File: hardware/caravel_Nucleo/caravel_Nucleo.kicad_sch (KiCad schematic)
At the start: 91 parts, among them J1 USB_B_Micro - 10118193-0001LF, J10 Conn_01x11_Female, J11 Conn_01x02, J12 Conn_01x02_Male, J2 Conn_01x02_Female, J3 Conn_01x02_Male, J4 Conn_01x04_Female, J5 Conn_01x02_Male, J6 Conn_01x02_Male, J7 Conn_01x06_Female, J8 Conn_01x03, J9 Conn_01x03, SW1 SW_Push - SKQGADE010, T1 Logo, T2 Logo, U1 FT232H, U10 MCP4661, U11 TAR5SxxU_SOT353F, U12 NUCLEO144-F746ZG, U2 SN74LVC1G125DCKR, U3 SN74LVC1G125DCKR, U4 MCP1319MT-29LE-OT, U5 TAR5SxxU_SOT353F, U6 TAR5SxxU_SOT353F, U7 W25Q32FVSS, U8 caravel_breakout, U9 MIC2211-AAYML-TR, X1 DSC6001_10MHZ, Y1 CSTNE12M0GH5L000R0

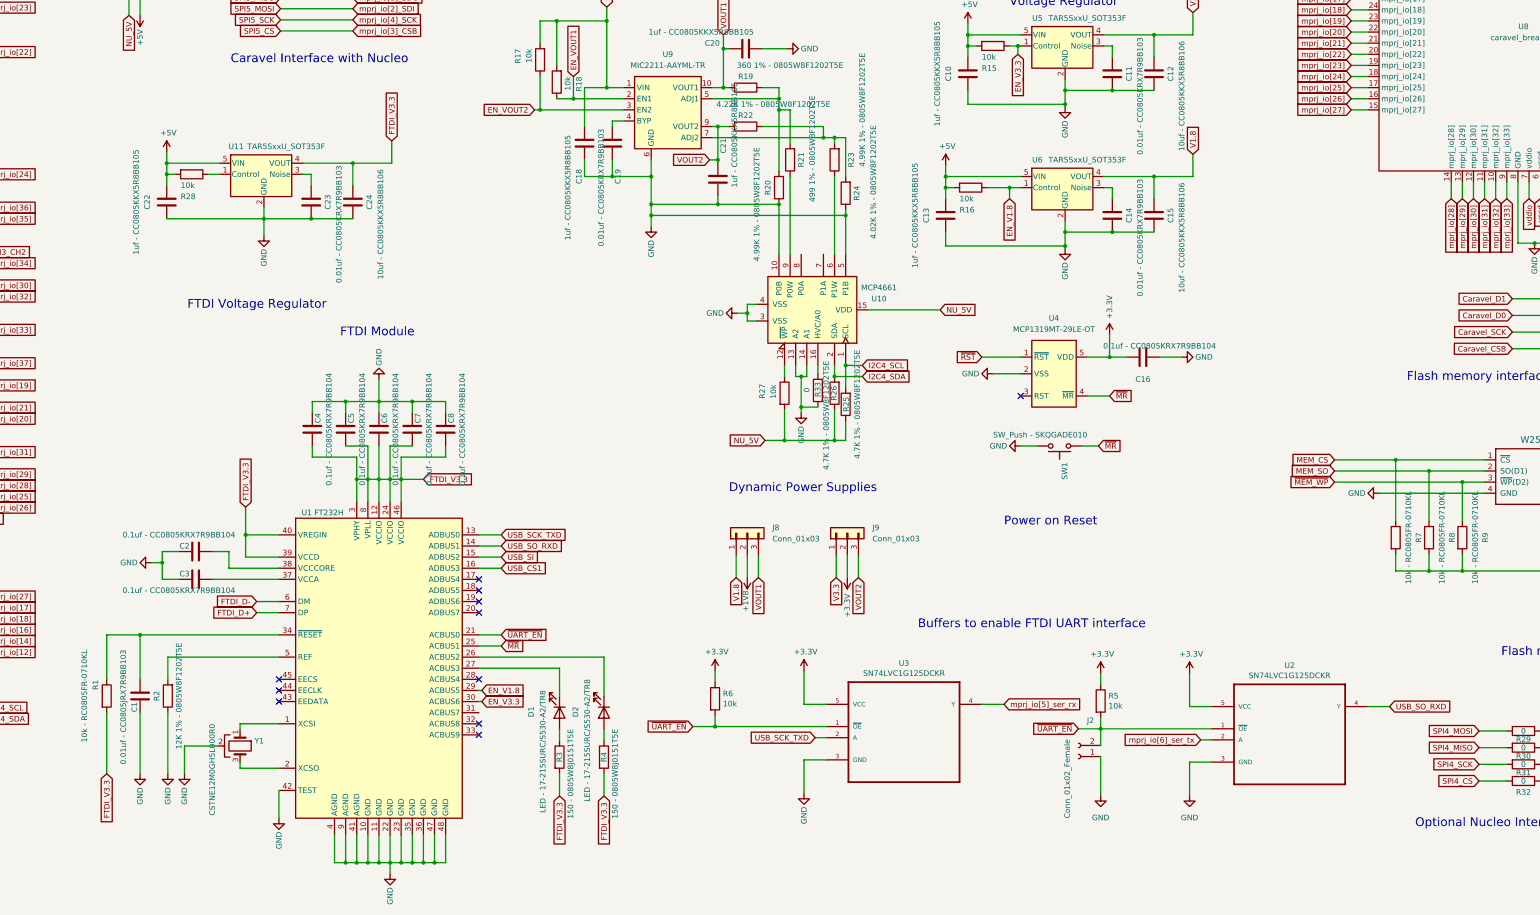
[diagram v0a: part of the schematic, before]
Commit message: Isolate FTDI scheamtic
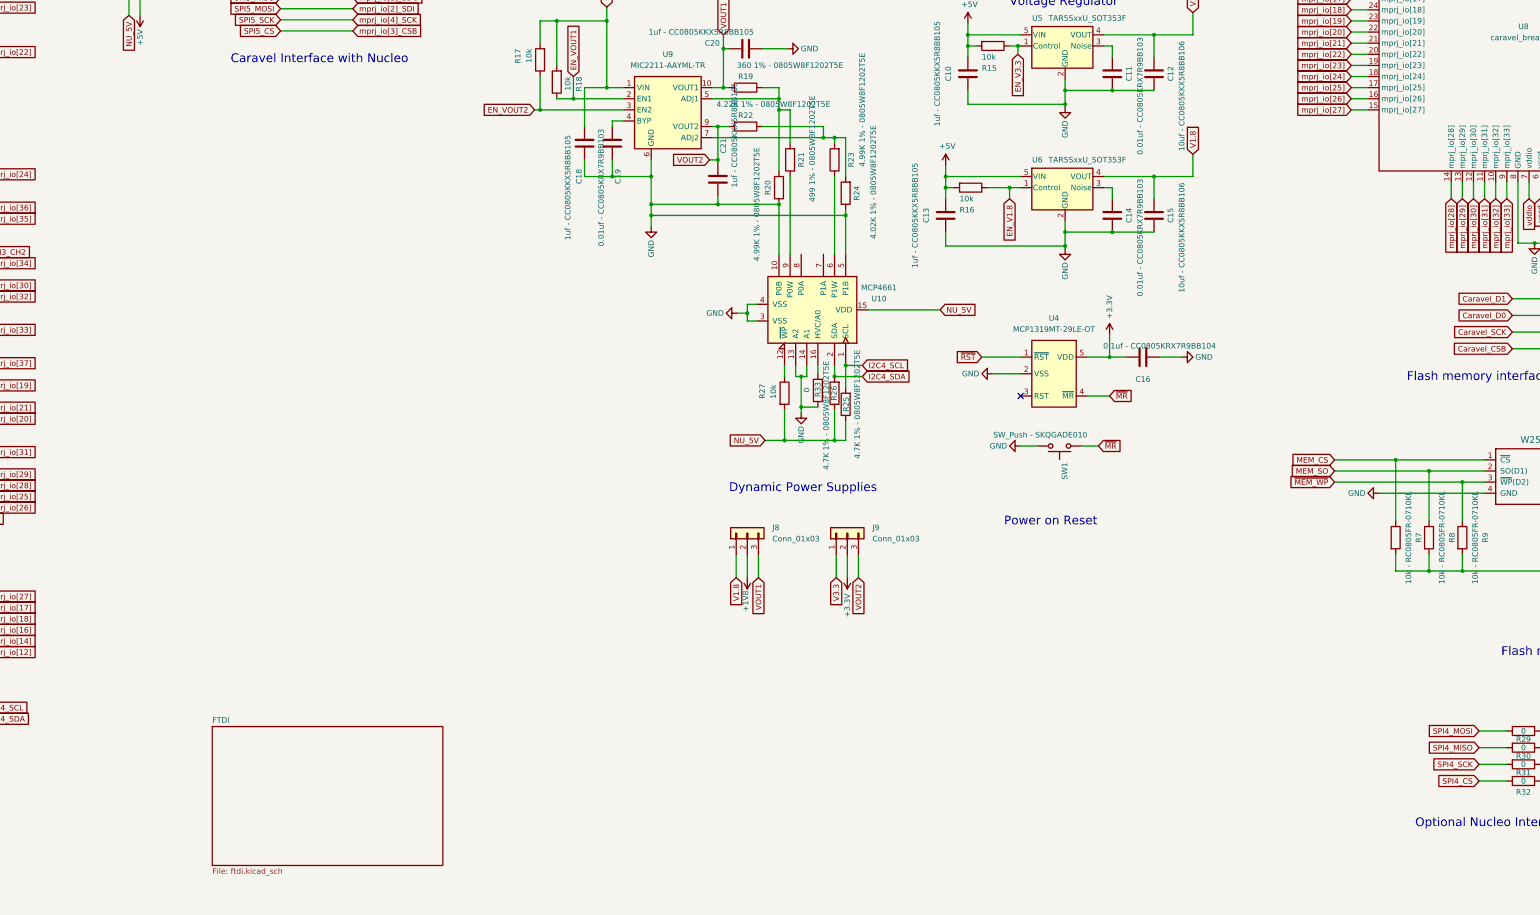
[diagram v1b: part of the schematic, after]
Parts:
- removed C1: 0.01uf - CC0805JRX7R9BB103, Capacitor_SMD:C_0805_2012Metric, symbol Device:C
- removed C2, C3, C4, C5, C6, C7, C8: 0.1uf - CC0805KRX7R9BB104, Capacitor_SMD:C_0805_2012Metric, symbol Device:C
- removed C22: 1uf - CC0805KKX5R8BB105, Capacitor_SMD:C_0805_2012Metric, symbol Device:C
- removed C23: 0.01uf - CC0805KRX7R9BB103, Capacitor_SMD:C_0805_2012Metric, symbol Device:C
- removed C24: 10uf - CC0805KKX5R8BB106, Capacitor_SMD:C_0805_2012Metric, symbol Device:C
- removed D1, D2: LED - 17-215SURC/S530-A2/TR8, LED_SMD:LED_1206_3216Metric, symbol Device:LED
- removed J2: Conn_01x02_Female, Connector_PinHeader_2.54mm:PinHeader_1x02_P2.54mm_Vertical, symbol Connector:Conn_01x02_Female
- removed R1: 10k - RC0805FR-0710KL, Resistor_SMD:R_0805_2012Metric, symbol Device:R
- removed R2: 12K 1% - 0805W8F1202T5E, Resistor_SMD:R_0805_2012Metric, symbol Device:R
- removed R28, R5, R6: 10k, Resistor_SMD:R_0805_2012Metric, symbol Device:R
- removed R3, R4: 150 - 0805W8J0151T5E, Resistor_SMD:R_0805_2012Metric, symbol Device:R
- removed U1: FT232H, Package_DFN_QFN:QFN-48-1EP_8x8mm_P0.5mm_EP6.2x6.2mm, symbol Interface_USB:FT232H
- removed U11: TAR5SxxU_SOT353F, Caravel_Board:SOT-353F, symbol Caravel_board:TAR5SxxU_SOT353F
- removed U2, U3: SN74LVC1G125DCKR, SOT65P210X110-5N, symbol Caravel_board:SN74LVC1G125DCKR
- removed Y1: CSTNE12M0GH5L000R0, strive_foot_prints:CSTNE12M0GH5L000R0, symbol Device:Crystal_GND2
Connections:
- no-connect marks 48 -> 38
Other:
- added sheet FTDI (ftdi.kicad_sch)
- note removed: "Buffers to enable FTDI UART interface"
- note removed: "FTDI Module"
- note removed: "FTDI Voltage Regulator"

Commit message: Substituted all components from main schematic sheet except Nucleo connector
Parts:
- removed C10, C13, C18, C20, C21: 1uf - CC0805KKX5R8BB105, Capacitor_SMD:C_0805_2012Metric, symbol Device:C
- removed C11, C14, C19: 0.01uf - CC0805KRX7R9BB103, Capacitor_SMD:C_0805_2012Metric, symbol Device:C
- removed C12, C15: 10uf - CC0805KKX5R8BB106, Capacitor_SMD:C_0805_2012Metric, symbol Device:C
- removed C16, C17, C9: 0.1uf - CC0805KRX7R9BB104, Capacitor_SMD:C_0805_2012Metric, symbol Device:C
- removed D3, D4: LED - 17-215SURC/S530-A2/TR8, LED_SMD:LED_1206_3216Metric, symbol Device:LED
- removed J1: USB_B_Micro - 10118193-0001LF, strive_foot_prints:FCI_10118193-0001LF, symbol Connector:USB_B_Micro
- removed J10: Conn_01x11_Female, Connector_PinHeader_2.54mm:PinHeader_1x11_P2.54mm_Vertical, symbol Connector:Conn_01x11_Female
- removed J11: Conn_01x02, Connector_PinHeader_2.54mm:PinHeader_1x02_P2.54mm_Vertical, symbol Connector_Generic:Conn_01x02
- removed J12, J3, J5, J6: Conn_01x02_Male, Connector_PinHeader_2.54mm:PinHeader_1x02_P2.54mm_Vertical, symbol Connector:Conn_01x02_Male
- removed J4: Conn_01x04_Female, Connector_PinHeader_2.54mm:PinHeader_1x04_P2.54mm_Vertical, symbol Connector:Conn_01x04_Female
- removed J7: Conn_01x06_Female, Connector_PinHeader_2.54mm:PinHeader_1x06_P2.54mm_Vertical, symbol Connector:Conn_01x06_Female
- removed J8, J9: Conn_01x03, Connector_PinHeader_2.54mm:PinHeader_1x03_P2.54mm_Vertical, symbol Connector_Generic:Conn_01x03
- removed R10, R11, R12, R7, R8, R9: 10k - RC0805FR-0710KL, Resistor_SMD:R_0805_2012Metric, symbol Device:R
- removed R13, R14: 82 - 0805W8F820JT5E, Resistor_SMD:R_0805_2012Metric, symbol Device:R
- removed R15, R16, R17, R18, R27: 10k, Resistor_SMD:R_0805_2012Metric, symbol Device:R
- removed R19: 360 1% - 0805W8F1202T5E, Resistor_SMD:R_0805_2012Metric, symbol Device:R
- removed R20, R23: 4.99K 1% - 0805W8F1202T5E, Resistor_SMD:R_0805_2012Metric, symbol Device:R
- removed R21: 499 1% - 0805W8F1202T5E, Resistor_SMD:R_0805_2012Metric, symbol Device:R
- removed R22: 4.22K 1% - 0805W8F1202T5E, Resistor_SMD:R_0805_2012Metric, symbol Device:R
- removed R24: 4.02K 1% - 0805W8F1202T5E, Resistor_SMD:R_0805_2012Metric, symbol Device:R
- removed R25, R26: 4.7K 1% - 0805W8F1202T5E, Resistor_SMD:R_0805_2012Metric, symbol Device:R
- removed R29, R30, R31, R32, R33: 0, Resistor_SMD:R_0805_2012Metric, symbol Device:R
- removed SW1: SW_Push - SKQGADE010, strive_foot_prints:SW4-SMD-5.2X5.2X1.5MM, symbol Switch:SW_Push
- removed TP1: TestPoint, TestPoint:TestPoint_Bridge_Pitch2.54mm_Drill1.0mm, symbol Connector:TestPoint
- removed U10: MCP4661, Package_DFN_QFN:QFN-16-1EP_5x5mm_P0.8mm_EP2.7x2.7mm, symbol Caravel_board:MCP4661
- removed U4: MCP1319MT-29LE-OT, Caravel_Board:PoR_5_SOT23, symbol Caravel_board:MCP1319MT-29LE-OT
- removed U5, U6: TAR5SxxU_SOT353F, Caravel_Board:SOT-353F, symbol Caravel_board:TAR5SxxU_SOT353F
- removed U7: W25Q32FVSS, strive_foot_prints:SOIC127P790X216-8N, symbol Caravel_board:W25Q32FVSS
- removed U8: caravel_breakout, Caravel_Board:caravel_breakout_flexy, symbol Caravel_board:caravel_breakout_v2
- removed U9: MIC2211-AAYML-TR, Package_DFN_QFN:DFN-10-1EP_3x3mm_P0.5mm_EP1.65x2.38mm, symbol Caravel_board:MIC2211-AAYML-TR
- removed X1: DSC6001_10MHZ, strive_foot_prints:DSC6001JE1A-010.0000, symbol Oscillator:XO91
- added C10, C13, C18, C20, C21: C_1u_0603, antmicro-footprints:0603-cap, symbol antmicroCapacitors0603:C_1u_0603
- added C11, C14, C19: C_10n_0603, antmicro-footprints:0603-cap, symbol antmicroCapacitors0603:C_10n_0603
- added C12, C15: C_10u_0603, antmicro-footprints:0603-cap, symbol antmicroCapacitors0603:C_10u_0603
- added C16, C17, C9: C_100n_0603, antmicro-footprints:0603-cap, symbol antmicroCapacitors0603:C_100n_0603
- added D3, D4: LTST-C150KGKT, antmicro-footprints:LED-1206, symbol antmicroLEDIndicationDiscrete:LTST-C150KGKT
- added J1: 10118193-0001LF, antmicro-footprints:USB_Micro_B_Female_10118193-0001LF, symbol antmicroUSBDVIHDMIConnectors:10118193-0001LF
- added J10: PinHeader_1x11, antmicro-footprints:PinHeader_1x11_P2.54_Vertical, symbol antmicroRectangularConnectorsHeadersMalePins:PinHeader_1x11
- added J11, J12, J3, J5, J6: PinHeader_1x02, antmicro-footprints:PinHeader_1x2_P2.54mm, symbol antmicroRectangularConnectorsHeadersMalePins:PinHeader_1x02
- added J4: 836-22-004-10-001101, antmicro-footprints:PogoPinHeader_1x4_P2mm_Drill1,5mm, symbol antmicroRectangularConnectorsHeadersMalePins:836-22-004-10-001101
- added J7: 836-22-006-10-001101, antmicro-footprints:PogoPinHeader_1x6_P2mm_Drill1,5mm, symbol antmicroRectangularConnectorsHeadersMalePins:836-22-006-10-001101
- added J8, J9: 640456-3, antmicro-footprints:PinHeader_1x3_P2.54_Drill1.1mm, symbol antmicroRectangularConnectorsHeadersMalePins:640456-3
- added R10, R11, R12, R15, R16, R17, R18, R27, R7, R8, R9: R_10k_0603, antmicro-footprints:0603-res, symbol antmicroResistors0603:R_10k_0603
- added R13, R14: R_82R_0603, antmicro-footprints:0603-res, symbol antmicroResistors0603:R_82R_0603
- added R19: R_360R_0603, antmicro-footprints:0603-res, symbol antmicroResistors0603:R_360R_0603
- added R20, R23: R_4k99_0603, antmicro-footprints:0603-res, symbol antmicroResistors0603:R_4k99_0603
- added R21: R_499R_0603, antmicro-footprints:0603-res, symbol antmicroResistors0603:R_499R_0603
- added R22: R_4k22_0603, antmicro-footprints:0603-res, symbol antmicroResistors0603:R_4k22_0603
- added R24: R_4k02_0402, antmicro-footprints:0402-res, symbol antmicroResistors0402:R_4k02_0402
- added R25, R26: R_4k7_0603, antmicro-footprints:0603-res, symbol antmicroResistors0603:R_4k7_0603
- added R29, R30, R31, R32, R33: R_0R_0603, antmicro-footprints:0603-res, symbol antmicroResistors0603:R_0R_0603
- added SW1: KMR2, antmicro-footprints:SW_SPST_4.2x2.8, symbol antmicroPushbuttonSwitches:KMR2
- added TP1: TP_SMD1MM, antmicro-footprints:Testpoint_smd_1mm, symbol antmicroTestPoints:TP_SMD1MM
- added U10: MCP4661, antmicro-footprints:QFN-16_EP_4x4_Pitch0.65mm, symbol antmicroInterfaceIOExpanders:MCP4661
- added U4: MAX811REUS+T, antmicro-footprints:SOT-143-4, symbol antmicroPMICPowerSequencers:MAX811REUS+T
- added U5: TAR5S33UTE85LF, antmicro-footprints:SOT-353, symbol antmicroPMICVoltageRegulatorsLinear:TAR5S33UTE85LF
- added U6: TAR5S18U(TE85L,F), antmicro-footprints:SOT-353, symbol antmicroPMICVoltageRegulatorsLinear:TAR5S18U(TE85L,F)
- added U7: W25Q32FVSS, antmicro-footprints:SOIC127P790X216-8N, symbol antmicroMemory:W25Q32FVSS
- added U8: caravel_breakout, antmicro-footprints:caravel_breakout, symbol antmicroModules:caravel_breakout
- added U9: MIC2211-AAYML-TR, antmicro-footprints:DFN-10-1EP_3x3mm, symbol antmicroPMICVoltageRegulatorsLinear:MIC2211-AAYML-TR
- added X1: ECS-2520MVLC-100-BN-TR, antmicro-footprints:Oscillator_SMD_ECS_2520MV-xxx-xx-4Pin_2.5x2.0mm, symbol antmicroCrystals:ECS-2520MVLC-100-BN-TR
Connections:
- net +1V8: now also J10.3, J10.4, J10.5, J3.1, J3.2, J8.2, U8.43 (vccd1), U8.50 (vccd), U8.6 (vccd)
- net +3V3: now also C16.1, C17.1, C9.2, J10.7, J10.8, J4.4, J5.1, J5.2, J9.2, R10.1, R11.1, R12.1, R13.1, R14.1, R7.1, R8.1, R9.1, U4.4 (VCC), U7.8 (VCC), U8.45 (vdda), U8.55 (vddio), U8.7 (vddio), X1.4 (VDD)
- net +5V: now also C10.1, C13.1, J1.1, J12.1, R15.1, R16.1, U5.5 (VIN), U6.5 (VIN)
- net Caravel_CSB: now also J7.1, R32.2, R7.2, U7.1 (~{CS}), U8.51 (Caravel_CSB)
- net Caravel_D0: now also J7.4, R10.2, R29.2, U7.5 (SI(D0)), U8.49 (Caravel_D0)
- net Caravel_D1: now also J7.2, R30.2, R8.2, U7.2 (SO(D1)), U8.48 (Caravel_D1)
- net Caravel_SCK: now also J7.5, R11.2, R31.2, U7.6 (SCK), U8.46 (Caravel_SCK)
- net EN_V1.8: now also R16.2, U6.1 (EN)
- net EN_V3.3: now also R15.2, U5.1 (EN)
- net EN_VOUT1: now also R18.1, U9.2 (EN1)
- net EN_VOUT2: now also R17.1, U9.3 (EN2)
- net FTDI_D+: now also J1.3
- net FTDI_D-: now also J1.2
- net GND: now also C10.2, C11.2, C12.2, C13.2, C14.2, C15.2, C16.2, C17.2, C18.2, C19.1, C20.2, C21.2, C9.1, D4.2, J1.5, J1.SH, J4.1, J6.2, R20.1, R24.1, R33.1, SW1.1, SW1.3, TP1.1, U10.10 (P0B), U10.13 (A2), U10.14 (A1), U10.3 (VSS), U10.4 (VSS), U10.5 (P1B), U4.1 (GND), U5.2 (GND), U6.2 (GND), U7.4 (GND), U8.5 (GND), U8.8 (GND), U9.6 (GND), X1.2 (GND)
- net I2C4_SCL: now also R25.2, U10.1 (SCL)
- net I2C4_SDA: now also R26.2, U10.2 (SDA)
- net NU_5V: now also C18.1, J12.2, R17.2, R18.2, R25.1, R26.1, R27.2, U10.15 (VDD), U9.1 (VIN)
- net SPI4_CS: now also R32.1
- net SPI4_MISO: now also R30.1
- net SPI4_MOSI: now also R29.1
- net SPI4_SCK: now also R31.1
- net SPI5_CS: now also U8.39 (mprj_io[3]_CSB)
- net SPI5_MISO: now also U8.41 (mprj_io[1]_SDO)
- net SPI5_MOSI: now also U8.40 (mprj_io[2]_SDI)
- net SPI5_SCK: now also U8.38 (mprj_io[4]_SCK)
- net TIM3_CH2: now also J11.2
- net UART8_RX: now also J4.3, U8.36 (mprj_io[6]_ser_tx)
- net UART8_TX: now also J4.2, U8.37 (mprj_io[5]_ser_rx)
- net V1.8: now also C15.1, J8.1, U6.4 (VOUT)
- net V3.3: now also C12.1, J9.1, U5.4 (VOUT)
- net VOUT1: now also C20.1, J8.3, R19.1, U9.10 (VOUT1)
- net VOUT2: now also C21.1, J9.3, R22.1, U9.9 (VOUT2)
- net gpio: now also D3.2, J10.10, U8.47 (gpio)
- net mprj_io[0]: now also U8.42 (mprj_io[0])
- net mprj_io[10]: now also U8.32 (mprj_io[10])
- net mprj_io[11]: now also U8.31 (mprj_io[11])
- net mprj_io[12]: now also U8.30 (mprj_io[12])
- net mprj_io[13]: now also U8.29 (mprj_io[13])
- net mprj_io[14]: now also U8.28 (mprj_io[14])
- net mprj_io[15]: now also U8.27 (mprj_io[15])
- net mprj_io[16]: now also U8.26 (mprj_io[16])
- net mprj_io[17]: now also U8.25 (mprj_io[17])
- net mprj_io[18]: now also U8.24 (mprj_io[18])
- net mprj_io[19]: now also U8.23 (mprj_io[19])
- net mprj_io[20]: now also U8.22 (mprj_io[20])
- net mprj_io[21]: now also U8.21 (mprj_io[21])
- net mprj_io[22]: now also U8.20 (mprj_io[22])
- net mprj_io[23]: now also U8.19 (mprj_io[23])
- net mprj_io[24]: now also U8.18 (mprj_io[24])
- net mprj_io[25]: now also U8.17 (mprj_io[25])
- net mprj_io[26]: now also U8.16 (mprj_io[26])
- net mprj_io[27]: now also U8.15 (mprj_io[27])
- net mprj_io[28]: now also U8.14 (mprj_io[28])
- net mprj_io[29]: now also U8.13 (mprj_io[29])
- net mprj_io[30]: now also U8.12 (mprj_io[30])
- net mprj_io[31]: now also U8.11 (mprj_io[31])
- net mprj_io[32]: now also U8.10 (mprj_io[32])
- net mprj_io[33]: now also U8.9 (mprj_io[33])
- net mprj_io[34]: now also U8.4 (mprj_io[34])
- net mprj_io[35]: now also U8.3 (mprj_io[35])
- net mprj_io[36]: now also U8.2 (mprj_io[36])
- net mprj_io[37]: now also U8.1 (mprj_io[37])
- net mprj_io[7]: now also U8.35 (mprj_io[7])
- net mprj_io[8]: now also U8.34 (mprj_io[8])
- net mprj_io[9]: now also U8.33 (mprj_io[9])
- net vccd2: now also J10.2, U8.56 (vccd2)
- net vdda1: now also J10.9, U8.44 (vdda1)
- net vdda2: now also J10.6, U8.54 (vdda2)
- net xclk: now also J10.11, J11.1, U8.52 (xclk), X1.3 (OUT)
- net ~{MEM_HOLD}: now also J7.6, R12.2, U7.7 (~{HOLD}(D3))
- net ~{MEM_WP}: now also J7.3, R9.2, U7.3 (~{WP}(D2))
- net ~{MR}: now also SW1.2, SW1.4, U4.3 (~{MR})
- net ~{RST}: now also J10.1, U4.2 (~{RST}), U8.53 (~{RST})
- new net: D3.1, R13.2
- new net: R21.1, U10.9 (P0W)
- new net: R19.2, R20.2, R21.2, U9.5 (ADJ1)
- new net: R27.1, U10.12 (~{WP})
- new net: R33.2, U10.16 (HVC/A0)
- new net: J6.1, X1.1 (EN)
- new net: C11.1, U5.3 (Noise)
- new net: C19.2, U9.4 (BYP)
- new net: R22.2, R23.2, R24.2, U9.7 (ADJ2)
- new net: R23.1, U10.6 (P1W)
- new net: D4.1, R14.2
- new net: C14.1, U6.3 (Noise)
- no-connect marks 38 -> 36
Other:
- moved on the sheet: U12
